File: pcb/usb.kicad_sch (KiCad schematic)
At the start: 0 parts

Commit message: WIP: power / battery schematic
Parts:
- added P1: USB_C_Plug_USB2.0, symbol Connector:USB_C_Plug_USB2.0
- added R1: 5k1, symbol Device:R
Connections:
- new net: P1.A4 (VBUS), P1.A9 (VBUS), P1.B4 (VBUS), P1.B9 (VBUS)
- new net GND: P1.A1 (GND), P1.A12 (GND), P1.B1 (GND), P1.B12 (GND), P1.S1 (SHIELD)
- new net USB_CC: P1.A5 (CC), R1.1
- new net USB_D+: P1.A6 (D+)
- new net USB_D-: P1.A7 (D-)
- no-connect marks 0 -> 1
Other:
- note added: "USB Rd resistor"

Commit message: WIP: power / battery schematic 2
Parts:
- removed P1: USB_C_Plug_USB2.0, symbol Connector:USB_C_Plug_USB2.0
- added D44: PRTR5V0U2X, Package_TO_SOT_SMD:SOT-143, symbol Power_Protection:PRTR5V0U2X
- added J2: USB_C_Receptacle, symbol Connector:USB_C_Receptacle
- added R2: 5k1, symbol Device:R
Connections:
- net GND: now also R1.2, D44.1 (GND), J2.A1 (GND), J2.A12 (GND), J2.B1 (GND), J2.B12 (GND), J2.S1 (SHIELD), R2.2
- net USB_D+: now also D44.3 (I/O2), J2.A6 (D+), J2.B6 (D+)
- net USB_D-: now also D44.2 (I/O1), J2.A7 (D-), J2.B7 (D-)
- net USB_CC: no longer names the net of R1.1
- net USB_CC: now also J2.A5 (CC1)
- new net: J2.A4 (VBUS), J2.A9 (VBUS), J2.B4 (VBUS), J2.B9 (VBUS)
- new net: J2.B5 (CC2), R2.1
- new net VBUS: D44.4 (VCC)
- no-connect marks 1 -> 10
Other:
- note added: "ESD protection for USB data lines"
- note removed: "USB Rd resistor"
- moved on the sheet: R1

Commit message: First version of power circuitry complete?
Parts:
- added BT1: Battery_Cell, symbol Device:Battery_Cell
- added C11: 10µF, symbol Device:C_Polarized
- added C18: 100nF, symbol Device:C
- added D64: MSS1P4-M3/89A, symbol Device:D_Schottky
- added D65, D66: LED, symbol Device:LED
- added Q1: FDN340P, Package_TO_SOT_SMD:SOT-23, symbol Transistor_FET:FDN340P
- added R3: 10k, symbol Device:R
- added R4, R5: 1k, symbol Device:R
- added R6: 0.4, symbol Device:R
- added R7: 2k2, symbol Device:R
- added TH1: NTC, symbol Device:Thermistor_NTC
- added U2: TP4056-42-ESOP8, Package_SO:SOIC-8-1EP_3.9x4.9mm_P1.27mm_EP2.41x3.3mm_ThermalVias, symbol Battery_Management:TP4056-42-ESOP8
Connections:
- net GND: now also BT1.2 (-), C11.2, C18.2, R3.1, R7.2, TH1.2, U2.3 (GND)
- net USB_VBUS: now reaches J2.A4 (VBUS), J2.A9 (VBUS), J2.B4 (VBUS), J2.B9 (VBUS)
- net USB_VBUS: now also D64.2 (A), Q1.1 (G), R3.2, R6.1
- new net: TH1.1, U2.1 (TEMP)
- new net: D66.1 (K), R5.1
- new net: C11.1, C18.1, D65.2 (A), D66.2 (A), R6.2, U2.4 (V_{CC}), U2.8 (CE)
- new net: D65.1 (K), R4.1
- new net: R4.2, U2.6 (~{STDBY})
- new net: R7.1, U2.2 (PROG)
- new net: R5.2, U2.7 (~{CHRG})
- new net BAT_POS: BT1.1 (+), Q1.2 (S), U2.5 (BAT)
- new net VDDH: D64.1 (K), Q1.3 (D)
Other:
- note added: "Battery Bypass"
- note added: "Battery Charger IC"
- note added: "Rprog = 2k2 => 1.15mA max current"
- note added: "Update when you choose an LED"

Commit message: Add an on/off switch
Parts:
- added SW2: SW_SPDT, symbol Switch:SW_SPDT
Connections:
- net VDDH: now also SW2.1 (A); no longer D64.1 (K), Q1.3 (D)
- new net: D64.1 (K), Q1.3 (D), SW2.2 (B)
- no-connect marks 10 -> 11
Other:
- note added: "On/Off switch"
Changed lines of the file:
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@@
+	)
+	(rectangle
+		(start 191.77 127)
+		(end 218.44 156.21)
+		(stroke
+			(width 0)
+			(type default)
+		)
+		(fill
+			(type none)
+		)
 	)
 	(rectangle
@@
 		)
 	)
+	(text "On/Off switch"
+		(exclude_from_sim no)
+		(at 199.644 129.54 0)
+		(effects
+			(font
+				(size 1.27 1.27)
+			)
+		)
+	)
 	(text "Battery Bypass"
 		(exclude_from_sim no)
@@
 	)
 	(no_connect
+		(at 205.74 147.32)
+	)
+	(no_connect
 		(at 62.23 85.09)
 	)
@@
 	(wire
 		(pts
+			(xy 210.82 142.24) (xy 205.74 142.24)
+		)
+		(stroke
+			(width 0)
+			(type default)
+		)
+	)
+	(wire
+		(pts
 			(xy 82.55 36.83) (xy 85.09 36.83)
 		)
@@
 	(wire
 		(pts
-			(xy 166.37 144.78) (xy 176.53 144.78)
+			(xy 166.37 144.78) (xy 195.58 144.78)
 		)
 		(stroke
@@
 	)
 	(symbol
-		(lib_id "power:VDD")
-		(at 176.53 144.78 0)
+		(lib_id "Switch:SW_SPDT")
+		(at 200.66 144.78 0)
 		(unit 1)
 		(exclude_from_sim no)
@@
 		(dnp no)
 		(fields_autoplaced yes)
-		(property "Reference" "#PWR032"
-			(at 176.53 148.59 0)
-			(effects
-				(font
-					(size 1.27 1.27)
-				)
-				(hide yes)
-			)
-		)
-		(property "Value" "VDDH"
-			(at 176.53 139.7 0)
+		(property "Reference" "SW2"
+			(at 200.66 135.89 0)
+			(effects
+				(font
+					(size 1.27 1.27)
+				)
+			)
+		)
+		(property "Value" "SW_SPDT"
+			(at 200.66 138.43 0)
 			(effects
 				(font
@@
 		)
 		(property "Footprint" ""
-			(at 176.53 144.78 0)
-			(effects
-				(font
-					(size 1.27 1.27)
-				)
-				(hide yes)
-			)
-		)
-		(property "Datasheet" ""
-			(at 176.53 144.78 0)
-			(effects
-				(font
-					(size 1.27 1.27)
-				)
-				(hide yes)
-			)
-		)
-		(property "Description" "Power symbol creates a global label with name \"VDD\""
-			(at 176.53 144.78 0)
-			(effects
-				(font
-					(size 1.27 1.27)
-				)
-				(hide yes)
-			)
+			(at 200.66 144.78 0)
+			(effects
+				(font
+					(size 1.27 1.27)
+				)
+				(hide yes)
+			)
+		)
+		(property "Datasheet" "~"
+			(at 200.66 152.4 0)
+			(effects
+				(font
+					(size 1.27 1.27)
+				)
+				(hide yes)
+			)
+		)
+		(property "Description" "Switch, single pole double throw"
+			(at 200.66 144.78 0)
+			(effects
+				(font
+					(size 1.27 1.27)
+				)
+				(hide yes)
+			)
+		)
+		(pin "3"
 		)
 		(pin "1"
+		)
+		(pin "2"
 		)
 		(instances
 			(project ""
 				(path "/39e5e398-89ad-4475-a3bf-05d3324a2c58/10482084-a545-4aa4-8b75-11043176cfae"
-					(reference "#PWR032")
+					(reference "SW2")
 					(unit 1)
 				)
@@
 					(unit 1)
 				)
+			)
+		)
+	)
+	(symbol
+		(lib_id "power:VDD")
+		(at 210.82 142.24 0)
+		(unit 1)
+		(exclude_from_sim no)
+		(in_bom yes)
+		(on_board yes)
+		(dnp no)
+		(property "Reference" "#PWR032"
+			(at 210.82 146.05 0)
+			(effects
+				(font
+					(size 1.27 1.27)
+				)
+				(hide yes)
+			)
+		)
+		(property "Value" "VDDH"
+			(at 210.82 137.16 0)
+			(effects
+				(font
+					(size 1.27 1.27)
+				)
+			)
+		)
+		(property "Footprint" ""
+			(at 210.82 142.24 0)
+			(effects
+				(font
+					(size 1.27 1.27)
+				)
+				(hide yes)
+			)
+		)
+		(property "Datasheet" ""
+			(at 210.82 142.24 0)
+			(effects
+				(font
+					(size 1.27 1.27)
+				)
+				(hide yes)
+			)
+		)
+		(property "Description" "Power symbol creates a global label with name \"VDD\""
+			(at 210.82 142.24 0)
+			(effects
+				(font
+					(size 1.27 1.27)
+				)
+				(hide yes)
+			)
+		)
+		(pin "1"
+		)
+		(instances
+			(project ""
+				(path "/39e5e398-89ad-4475-a3bf-05d3324a2c58/10482084-a545-4aa4-8b75-11043176cfae"
+					(reference "#PWR032")
+					(unit 1)
+				)

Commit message: Start assigning footprints
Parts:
- C11: footprint (none) -> Capacitor_Tantalum_SMD:CP_EIA-2012-15_AVX-P_HandSolder
- C18: footprint (none) -> Capacitor_SMD:C_0805_2012Metric_Pad1.18x1.45mm_HandSolder
- D65, D66: footprint (none) -> LED_SMD:LED_0805_2012Metric_Pad1.15x1.40mm_HandSolder
- R1, R2, R3, R4, R5, R6, R7: footprint (none) -> Resistor_SMD:R_0805_2012Metric_Pad1.20x1.40mm_HandSolder
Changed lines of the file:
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@@
 			)
 		)
-		(property "Footprint" ""
+		(property "Footprint" "LED_SMD:LED_0805_2012Metric_Pad1.15x1.40mm_HandSolder"
 			(at 151.13 58.42 0)
 			(effects
@@
 			)
 		)
-		(property "Footprint" ""
+		(property "Footprint" "Resistor_SMD:R_0805_2012Metric_Pad1.20x1.40mm_HandSolder"
 			(at 78.74 38.608 90)
 			(effects
@@
 			)
 		)
-		(property "Footprint" ""
+		(property "Footprint" "Resistor_SMD:R_0805_2012Metric_Pad1.20x1.40mm_HandSolder"
 			(at 135.89 138.938 90)
 			(effects
@@
 			)
 		)
-		(property "Footprint" ""
+		(property "Footprint" "Capacitor_Tantalum_SMD:CP_EIA-2012-15_AVX-P_HandSolder"
 			(at 115.2652 54.61 0)
 			(effects
@@
 			)
 		)
-		(property "Footprint" ""
+		(property "Footprint" "Resistor_SMD:R_0805_2012Metric_Pad1.20x1.40mm_HandSolder"
 			(at 139.192 69.85 90)
 			(effects
@@
 			)
 		)
-		(property "Footprint" ""
+		(property "Footprint" "Resistor_SMD:R_0805_2012Metric_Pad1.20x1.40mm_HandSolder"
 			(at 172.212 40.64 90)
 			(effects
@@
 			)
 		)
-		(property "Footprint" ""
+		(property "Footprint" "Capacitor_SMD:C_0805_2012Metric_Pad1.18x1.45mm_HandSolder"
 			(at 129.2352 54.61 0)
 			(effects
@@
 			)
 		)
-		(property "Footprint" ""
+		(property "Footprint" "Resistor_SMD:R_0805_2012Metric_Pad1.20x1.40mm_HandSolder"
 			(at 149.352 69.85 90)
 			(effects
@@
 			)
 		)
-		(property "Footprint" ""
+		(property "Footprint" "Resistor_SMD:R_0805_2012Metric_Pad1.20x1.40mm_HandSolder"
 			(at 78.74 46.228 90)
 			(effects
@@
 			)
 		)
-		(property "Footprint" ""
+		(property "Footprint" "Resistor_SMD:R_0805_2012Metric_Pad1.20x1.40mm_HandSolder"
 			(at 182.372 81.28 90)
 			(effects
@@
 			)
 		)
-		(property "Footprint" ""
+		(property "Footprint" "LED_SMD:LED_0805_2012Metric_Pad1.15x1.40mm_HandSolder"
 			(at 140.97 58.42 0)
 			(effects

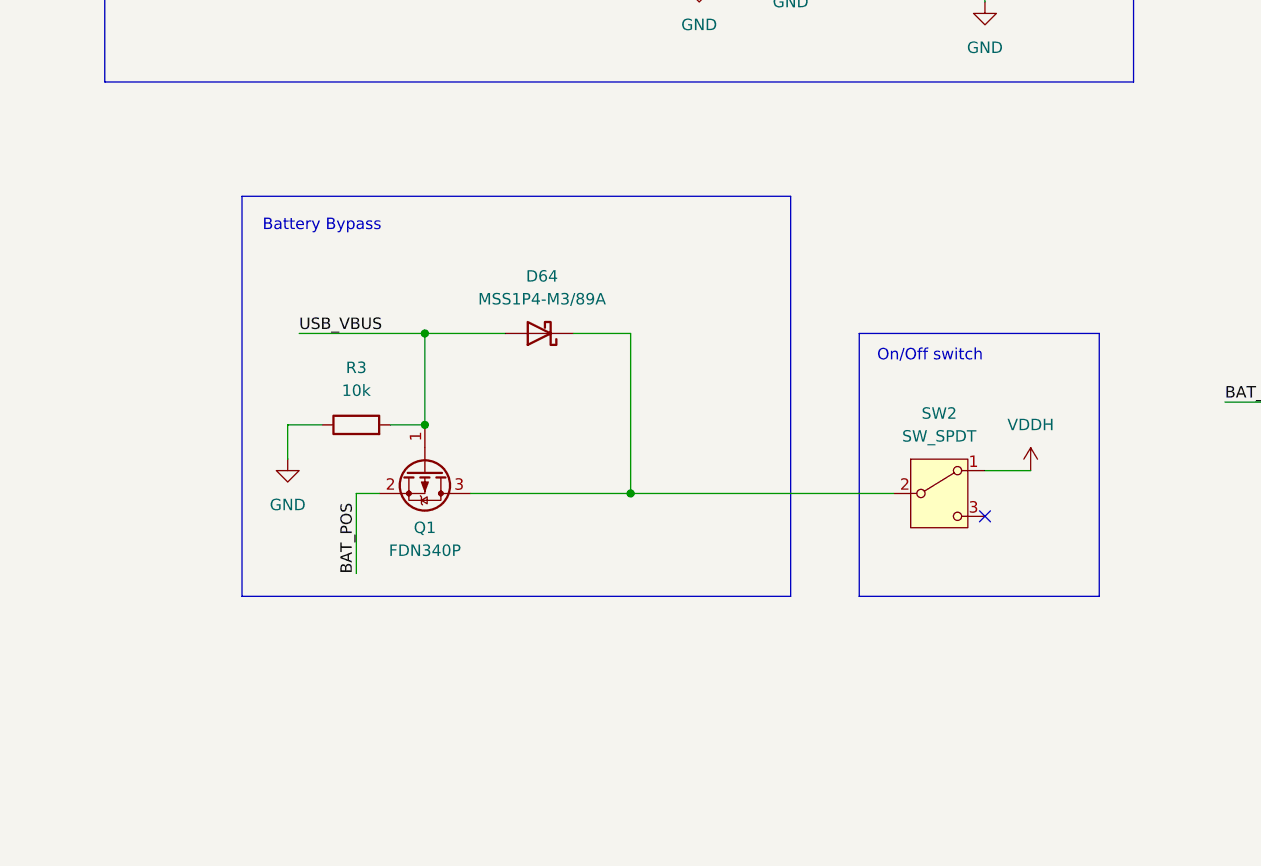
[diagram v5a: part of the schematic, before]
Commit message: Fix MOSFET orientation
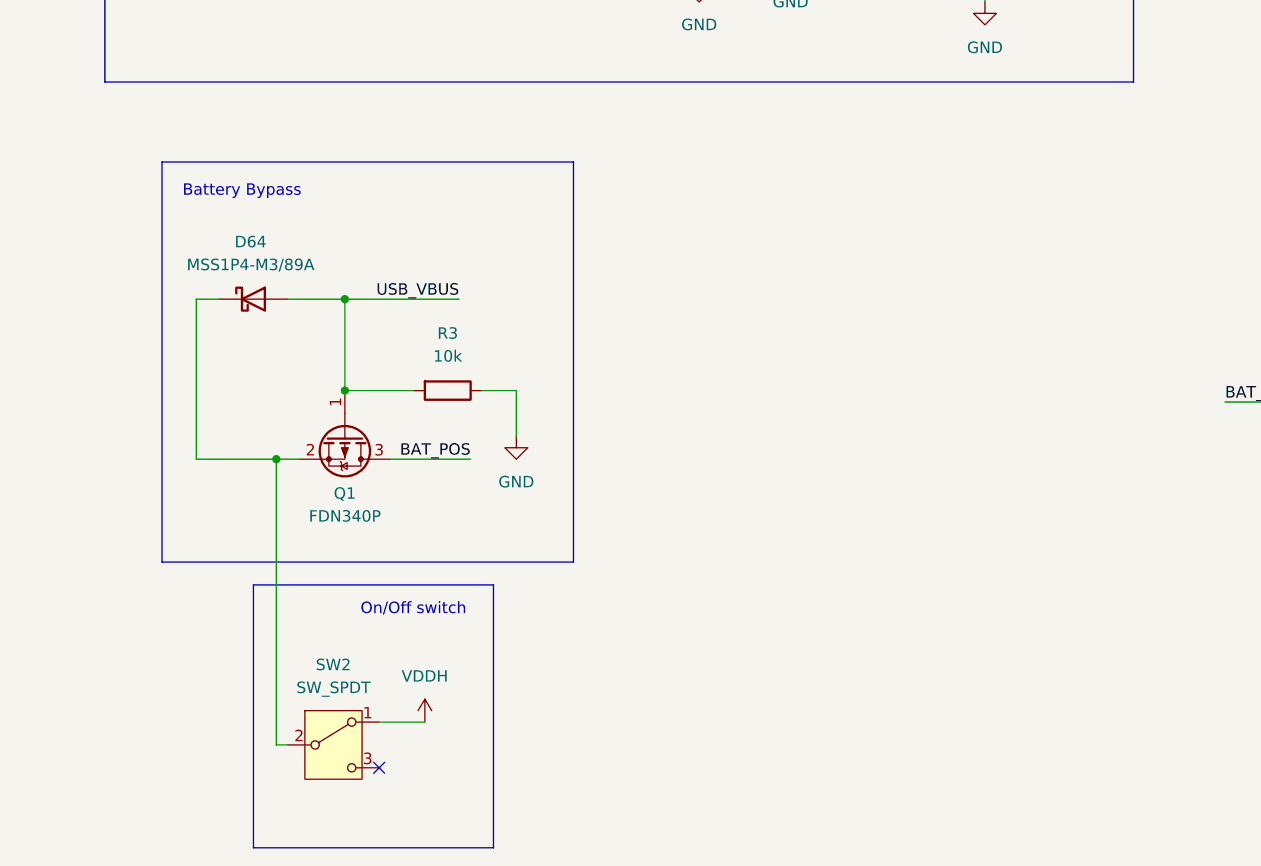
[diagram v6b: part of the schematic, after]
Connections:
- net BAT_POS: now also Q1.3 (D); no longer Q1.2 (S)
- net at D64.1 (K), SW2.2 (B): now also Q1.2 (S); no longer Q1.3 (D)
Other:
- moved on the sheet: D64, Q1, R3, SW2

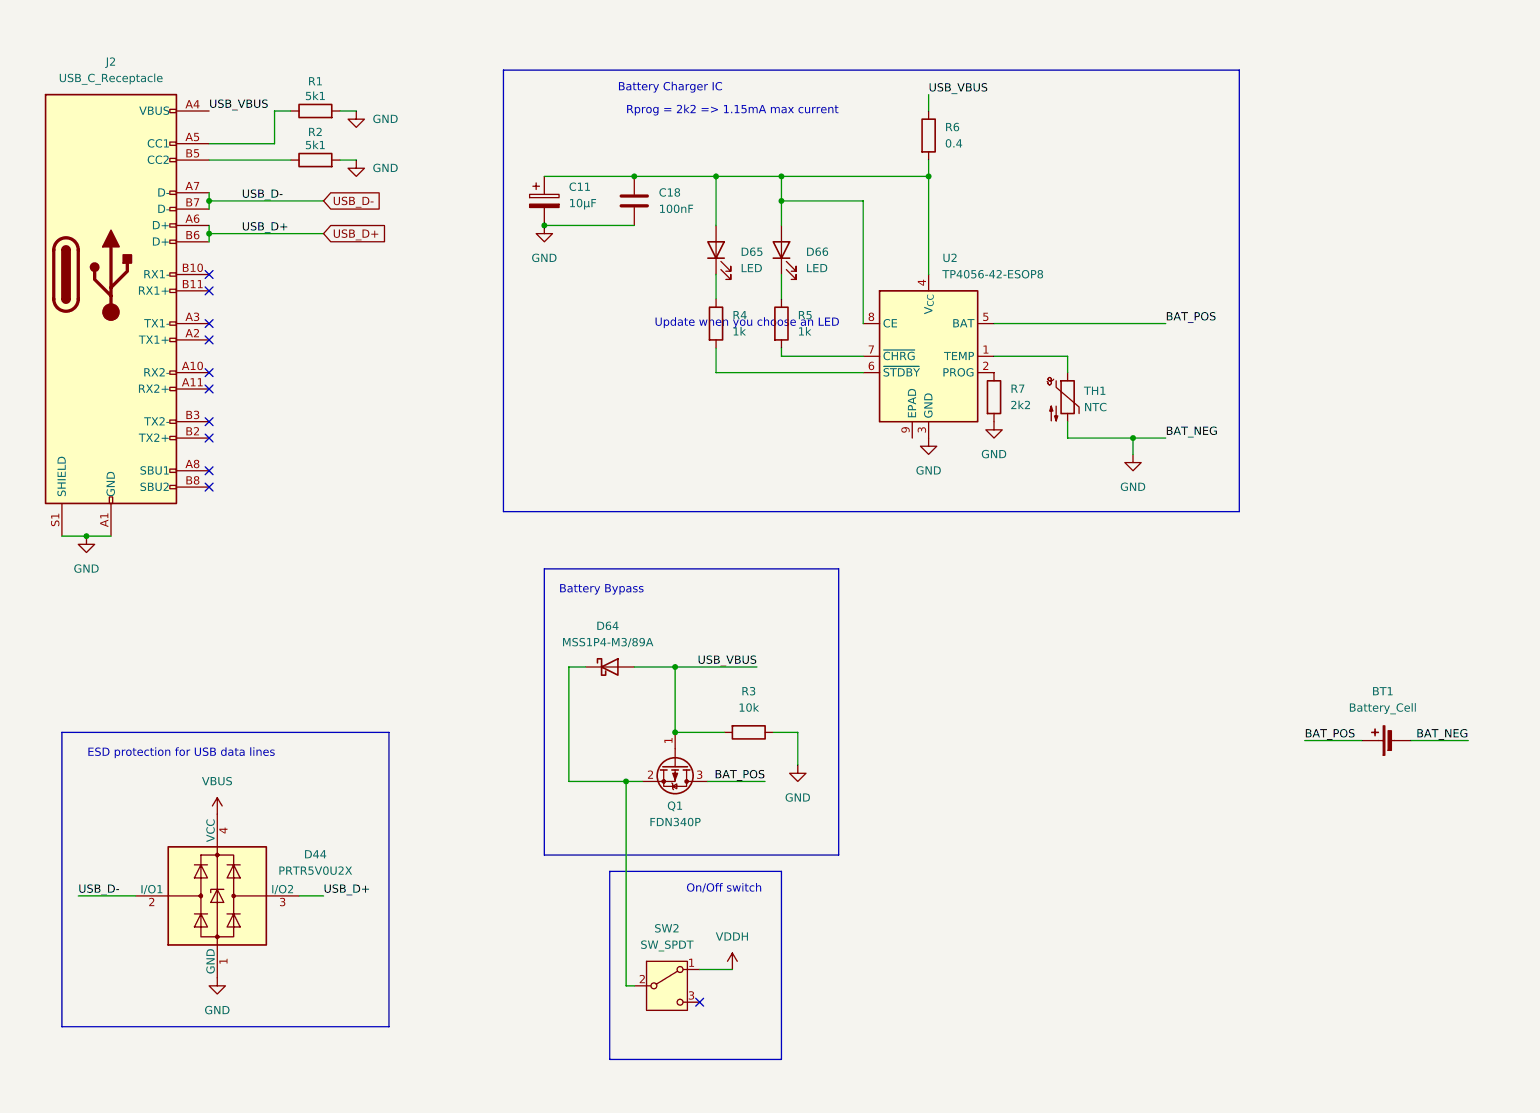
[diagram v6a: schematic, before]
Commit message: Add battery protection IC
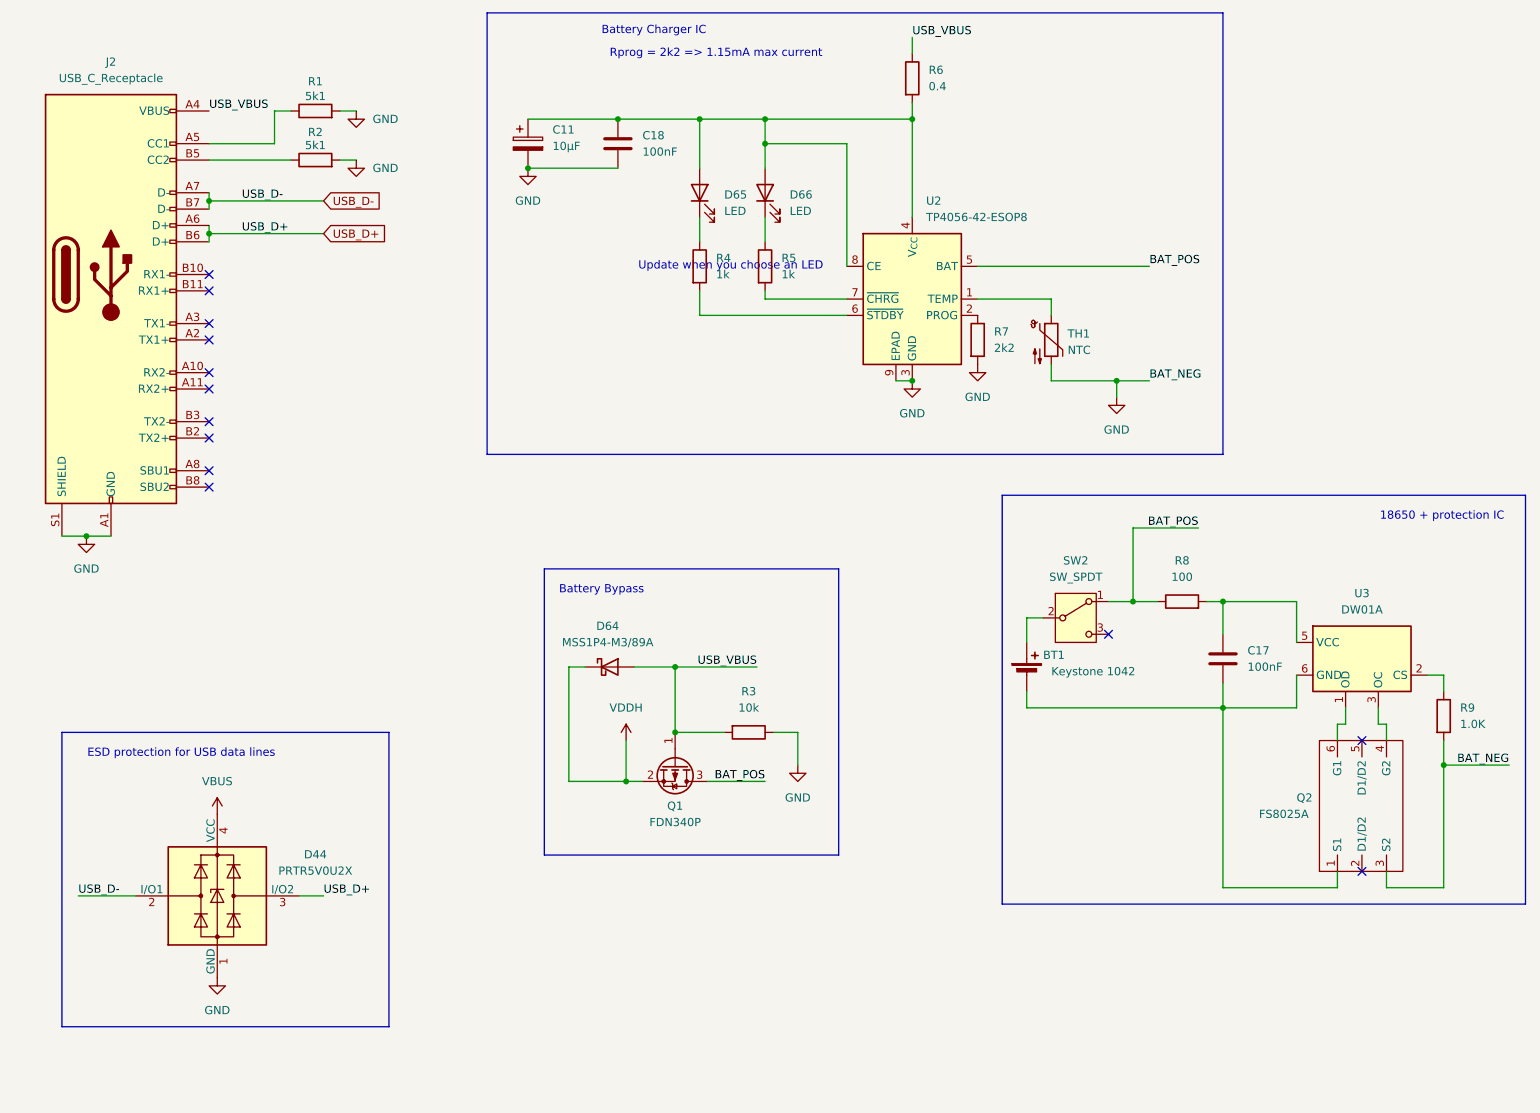
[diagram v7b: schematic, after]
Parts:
- added C17: 100nF, symbol Device:C
- added Q2: FS8025A, symbol my_symbols:FS8025A
- added R8: 100, symbol Device:R
- added R9: 1.0K, symbol Device:R
- added U3: DW01A, Package_TO_SOT_SMD:SOT-23-6, symbol Battery_Management:DW01A
- BT1: value Battery_Cell -> Keystone 1042
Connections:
- net BAT_POS: now also SW2.1 (A), R8.1; no longer BT1.1 (+)
- net GND: now also U2.9 (EPAD), Q2.3 (S2), R9.2; no longer BT1.2 (-)
- net VDDH: now also D64.1 (K), Q1.2 (S); no longer SW2.1 (A)
- new net: Q2.6 (G1), U3.1 (OD)
- new net: R9.1, U3.2 (CS)
- new net: Q2.4 (G2), U3.3 (OC)
- new net: C17.1, R8.2, U3.5 (VCC)
- new net: BT1.2 (-), C17.2, Q2.1 (S1), U3.6 (GND)
- new net: BT1.1 (+), SW2.2 (B)
- no-connect marks 11 -> 13
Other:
- note added: "18650 + protection IC"
- note removed: "On/Off switch"
- moved on the sheet: BT1, C11, C18, D65, D66, R4, R5, R6, R7, SW2, TH1, U2
